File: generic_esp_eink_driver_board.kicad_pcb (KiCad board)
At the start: 2 copper layers, 160 x 25 mm, 53 parts, among them IC1 TPS7A0233PDBVR, IC2 MAX17260SETD+T, J1 USB_C_Receptacle_USB2.0_16P, J2 S2B-PH-SM4-TB, J3 Conn_01x04, Q1 AO3400A, U1 USBLC6-2SC6, U2 BQ24040DSQR, U3 ESP32-S3-WROOM-1, U4 FPC24

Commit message: New layout
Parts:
- moved IC2 41.5 mm to (75.6, 78.1), turned to 180 degrees
- moved C8 36.6 mm to (75.3, 75.2), turned to 0 degrees
- moved R8 33.7 mm to (80.0, 79.0)
- moved C7 32.4 mm to (80.0, 76.8), turned to 0 degrees
- moved IC1 21.5 mm to (110.5, 81.2)
- moved R7 19.0 mm to (88.8, 71.0), turned to 0 degrees
- moved C2 17.2 mm to (70.5, 86.2), turned to 180 degrees
- moved C1 15.6 mm to (67.2, 87.3), turned to 90 degrees
- moved C3 15.4 mm to (80.0, 74.5), turned to 180 degrees
- moved BOOT1 15.3 mm to (82.1, 85.5)
- moved ENABLE1 15.3 mm to (75.5, 85.5)
- moved R3 15.0 mm to (84.0, 79.0), turned to 0 degrees
- moved U4 14.2 mm to (125.5, 68.3)
- moved U2 13.9 mm to (84.5, 74.8)
- moved C20 13.4 mm to (99.2, 75.0), turned to -90 degrees
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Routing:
- net 3V3: track 0.00 -> 12.6 mm
- net Net-(C18-Pad2): track 0.00 -> 8.48 mm
- net Net-(C19-Pad2): track 0.00 -> 6.77 mm
- net Net-(D5-A): track 0.00 -> 6.52 mm
- net Net-(R11-Pad2): track 0.00 -> 6.02 mm
- net Net-(C15-Pad2): track 0.00 -> 5.17 mm
- net EN: track 0.00 -> 4.63 mm
- net Net-(C11-Pad2): track 0.00 -> 4.23 mm
- net Net-(C14-Pad2): track 0.00 -> 3.46 mm
- net Net-(C12-Pad2): track 0.00 -> 2.96 mm
- net Net-(C13-Pad2): track 0.00 -> 2.83 mm
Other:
- outline, holes or cut-outs redrawn

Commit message: re-placement
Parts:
- added C21: 100nF, Capacitor_SMD:C_0805_2012Metric_Pad1.18x1.45mm_HandSolder, F.Cu at (70.2, 73.2)
- added J4: Micro_SD_Card_Det_Hirose_DM3AT, Connector_Card:microSD_HC_Hirose_DM3AT-SF-PEJM5, F.Cu at (64.2, 84.2)
- added R13: 10k, Resistor_SMD:R_0805_2012Metric_Pad1.20x1.40mm_HandSolder, F.Cu at (68.2, 73.2)
- added R14: 10k, Resistor_SMD:R_0805_2012Metric_Pad1.20x1.40mm_HandSolder, F.Cu at (66.2, 73.2)
- added R15: 10k, Resistor_SMD:R_0805_2012Metric_Pad1.20x1.40mm_HandSolder, F.Cu at (64.2, 73.2)
- added R16: 10k, Resistor_SMD:R_0805_2012Metric_Pad1.20x1.40mm_HandSolder, F.Cu at (62.2, 73.2)
- added R17: 10k, Resistor_SMD:R_0805_2012Metric_Pad1.20x1.40mm_HandSolder, F.Cu at (60.2, 73.2)
- added R18: 10k, Resistor_SMD:R_0805_2012Metric_Pad1.20x1.40mm_HandSolder, F.Cu at (58.2, 73.2)
- moved J3 47.0 mm to (117.5, 97.5)
- moved C5 42.7 mm to (95.6, 92.1), turned to 0 degrees
- moved C6 40.5 mm to (95.6, 90.1), turned to 0 degrees
- moved J1 39.9 mm to (129.4, 95.9)
- moved R4 38.4 mm to (95.6, 88.1), turned to 180 degrees
- moved C4 36.4 mm to (95.6, 86.1), turned to 0 degrees
- moved C3 36.2 mm to (115.4, 81.9), turned to 0 degrees
- moved U1 35.0 mm to (121.2, 92.5)
- moved R9 32.2 mm to (133.9, 82.5), turned to 0 degrees
- moved C9 31.2 mm to (125.8, 85.5), turned to 0 degrees
- moved R8 31.1 mm to (110.5, 85.0), turned to 90 degrees
- moved U2 30.5 mm to (113.4, 84.6), turned to -90 degrees
- moved IC2 30.2 mm to (105.0, 85.0)
- moved R10 30.1 mm to (133.9, 80.0), turned to 180 degrees
- moved C7 29.6 mm to (108.5, 85.0), turned to -90 degrees
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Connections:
- R7 pad 1: Net-(U3-IO39) -> Net-(U3-IO4)
- U3 pad 24: unconnected-(U3-IO47-Pad24) -> SD_D1
- U3 pad 25: unconnected-(U3-IO48-Pad25) -> SD_DET
- U3 pad 31: unconnected-(U3-IO38-Pad31) -> SD_D2
- U3 pad 32: Net-(U3-IO39) -> SD_D3
- U3 pad 33: unconnected-(U3-IO40-Pad33) -> SD_CMD
- U3 pad 34: unconnected-(U3-IO41-Pad34) -> SD_CLK
- U3 pad 35: unconnected-(U3-IO42-Pad35) -> SD_D0
- U3 pad 4: unconnected-(U3-IO4-Pad4) -> Net-(U3-IO4)
- U3 pad 8: FG_SDA -> FG_SCL
- U3 pad 9: FG_SCL -> FG_SDA
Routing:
- net Net-(C18-Pad2): track 8.48 -> 0.00 mm
- net Net-(C19-Pad2): track 6.77 -> 0.00 mm
- net Net-(D5-A): track 6.52 -> 0.00 mm
- net Net-(R11-Pad2): track 6.02 -> 0.00 mm
- net 3V3: track 12.6 -> 7.16 mm
- net Net-(C15-Pad2): track 5.17 -> 0.00 mm
- net Net-(C11-Pad2): track 4.23 -> 0.00 mm
- net Net-(C14-Pad2): track 3.46 -> 0.00 mm
- net Net-(C12-Pad2): track 2.96 -> 0.00 mm
- net Net-(C13-Pad2): track 2.83 -> 0.00 mm
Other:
- board size 160 x 25 mm -> 170 x 35 mm
- board text added: "Battery"

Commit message: Route SD card
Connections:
- U3 pad 24: SD_D1 -> unconnected-(U3-IO47-Pad24)
- U3 pad 25: SD_DET -> unconnected-(U3-IO48-Pad25)
- U3 pad 38: unconnected-(U3-IO2-Pad38) -> SD_D1
- U3 pad 39: unconnected-(U3-IO1-Pad39) -> SD_DET
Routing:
- net SD_DET: track 0.00 -> 29.2 mm
- net SD_D1: track 0.00 -> 25.5 mm
- net SD_D0: track 0.00 -> 21.1 mm
- net SD_CLK: track 0.00 -> 18.5 mm
- net EN: track 4.63 -> 21.7 mm
- net SD_CMD: track 0.00 -> 16.0 mm
- net SD_D3: track 0.00 -> 13.9 mm
- net SD_D2: track 0.00 -> 13.0 mm
- net BOOT: track 0.00 -> 12.2 mm
- net 3V3: track 7.16 -> 19.2 mm
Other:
- board size 170 x 35 mm -> 170 x 47.2 mm

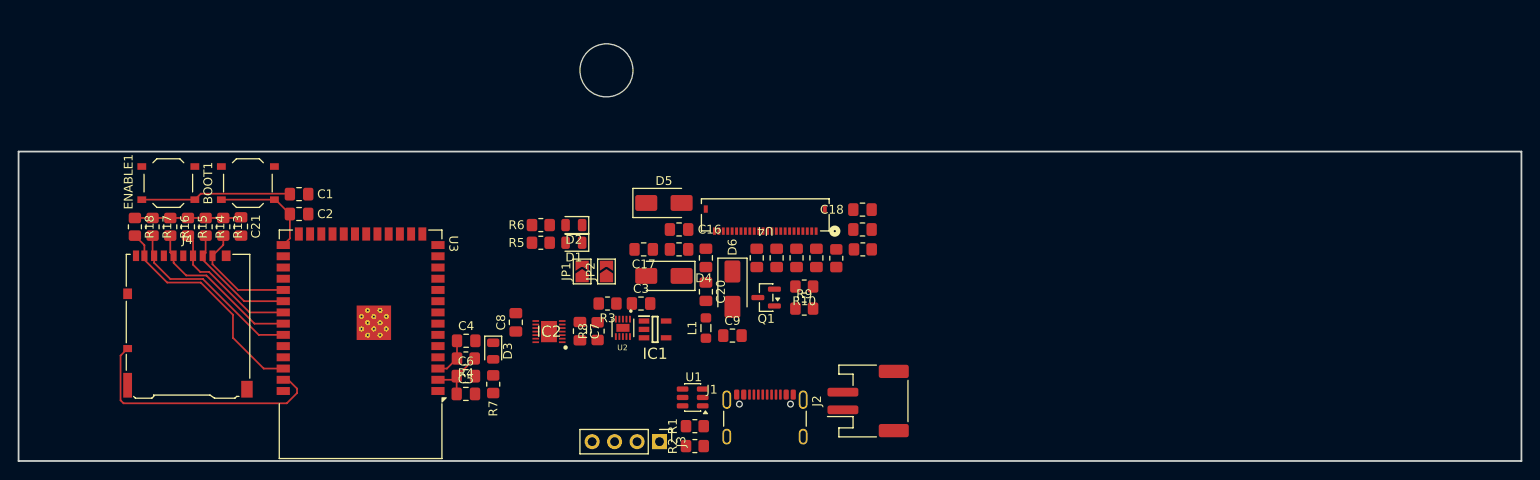
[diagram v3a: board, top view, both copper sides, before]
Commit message: Add temp/hum sensor
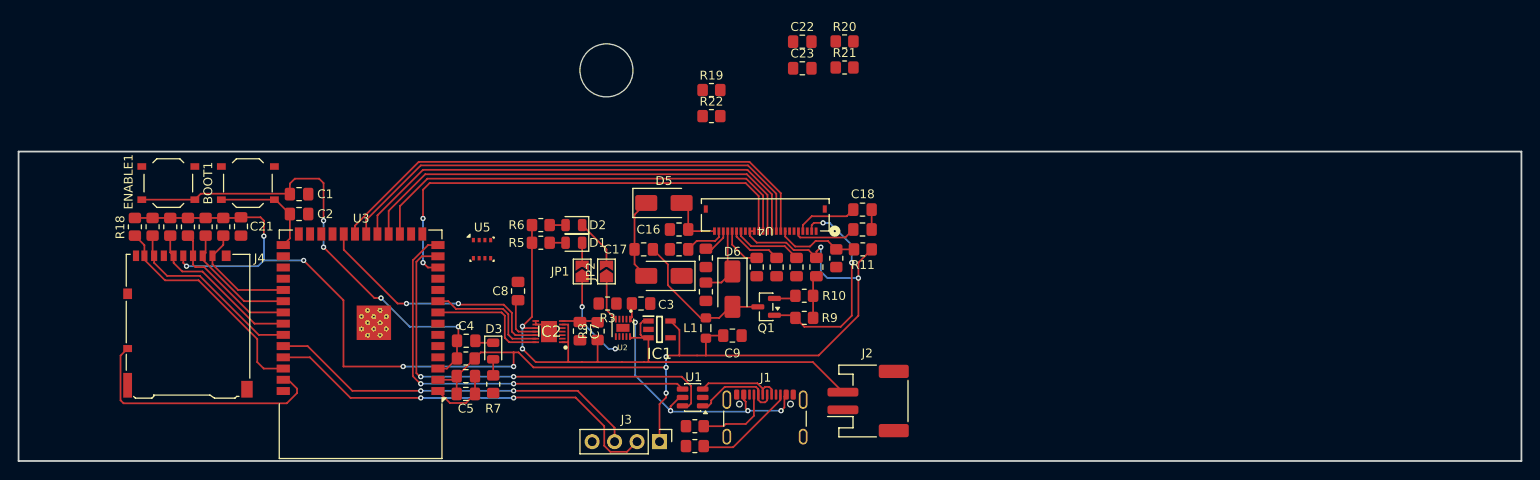
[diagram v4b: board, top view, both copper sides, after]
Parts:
- added C22: 0.1uF, Capacitor_SMD:C_0805_2012Metric_Pad1.18x1.45mm_HandSolder, F.Cu at (133.7, 52.3)
- added C23: 0.1uF, Capacitor_SMD:C_0805_2012Metric_Pad1.18x1.45mm_HandSolder, F.Cu at (133.7, 55.3)
- added R19: 10k, Resistor_SMD:R_0805_2012Metric_Pad1.20x1.40mm_HandSolder, F.Cu at (123.4, 57.7)
- added R20: 4.7k, Resistor_SMD:R_0805_2012Metric_Pad1.20x1.40mm_HandSolder, F.Cu at (138.4, 52.2)
- added R21: 4.7k, Resistor_SMD:R_0805_2012Metric_Pad1.20x1.40mm_HandSolder, F.Cu at (138.4, 55.2)
- added R22: 10k, Resistor_SMD:R_0805_2012Metric_Pad1.20x1.40mm_HandSolder, F.Cu at (123.4, 60.7)
- added U5: BME280, Package_LGA:Bosch_LGA-8_2.5x2.5mm_P0.65mm_ClockwisePinNumbering, F.Cu at (97.4, 75.7)
- moved C8 3.55 mm to (101.5, 80.5)
- moved Q1 1.05 mm to (129.6, 82.2)
- moved R10 1.05 mm to (133.9, 81.0)
- moved R9 1.05 mm to (133.9, 83.5)
- moved C10 1.04 mm to (135.2, 77.8)
- moved C11 1.04 mm to (133.0, 77.8)
- moved C12 1.04 mm to (130.8, 77.8)
- moved C13 1.04 mm to (128.5, 77.8)
- moved IC1 0.50 mm to (117.5, 84.8)
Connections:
- net FG_SCL renamed FG_SCK
- U3 pad 11: unconnected-(U3-IO18-Pad11) -> TEMP_PWR
- U3 pad 12: DISP_BUSY -> DISP_SDA
- U3 pad 17: DISP_RESET -> DISP_SCL
- U3 pad 18: DISP_DATA -> DISP_CS
- U3 pad 19: DISP_CS -> DISP_DATA
- U3 pad 20: DISP_SCL -> DISP_RESET
- U3 pad 21: DISP_SDA -> DISP_BUSY
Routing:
- net 3V3: track 19.2 -> 167.6 mm, vias 0 -> 10
- net VBAT: track 0.00 -> 70.7 mm, vias 0 -> 2
- net DISP_BUSY: track 0.00 -> 57.9 mm
- net DISP_RESET: track 0.00 -> 56.1 mm
- net DISP_DATA: track 0.00 -> 54.2 mm
- net DISP_SDA: track 0.00 -> 53.0 mm, vias 0 -> 2
- net DISP_CS: track 0.00 -> 52.3 mm
- net DISP_SCL: track 0.00 -> 50.3 mm
- net USB_D-: track 0.00 -> 50.0 mm, vias 0 -> 2
- net USB_D+: track 0.00 -> 47.8 mm, vias 0 -> 2
- net Net-(J3-Pin_2): track 0.00 -> 46.3 mm, vias 0 -> 2
- net Net-(J3-Pin_3): track 0.00 -> 43.0 mm, vias 0 -> 2
- net EN: track 21.7 -> 55.0 mm, vias 0 -> 4
- net VBUS: track 0.00 -> 33.2 mm, vias 0 -> 4
- net FG_ALARM: track 0.00 -> 28.7 mm, vias 0 -> 2
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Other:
- board text removed: "Board height 25mm"
- board text removed: "Board length 160mm"
